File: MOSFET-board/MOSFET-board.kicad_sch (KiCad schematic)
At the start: 64 parts

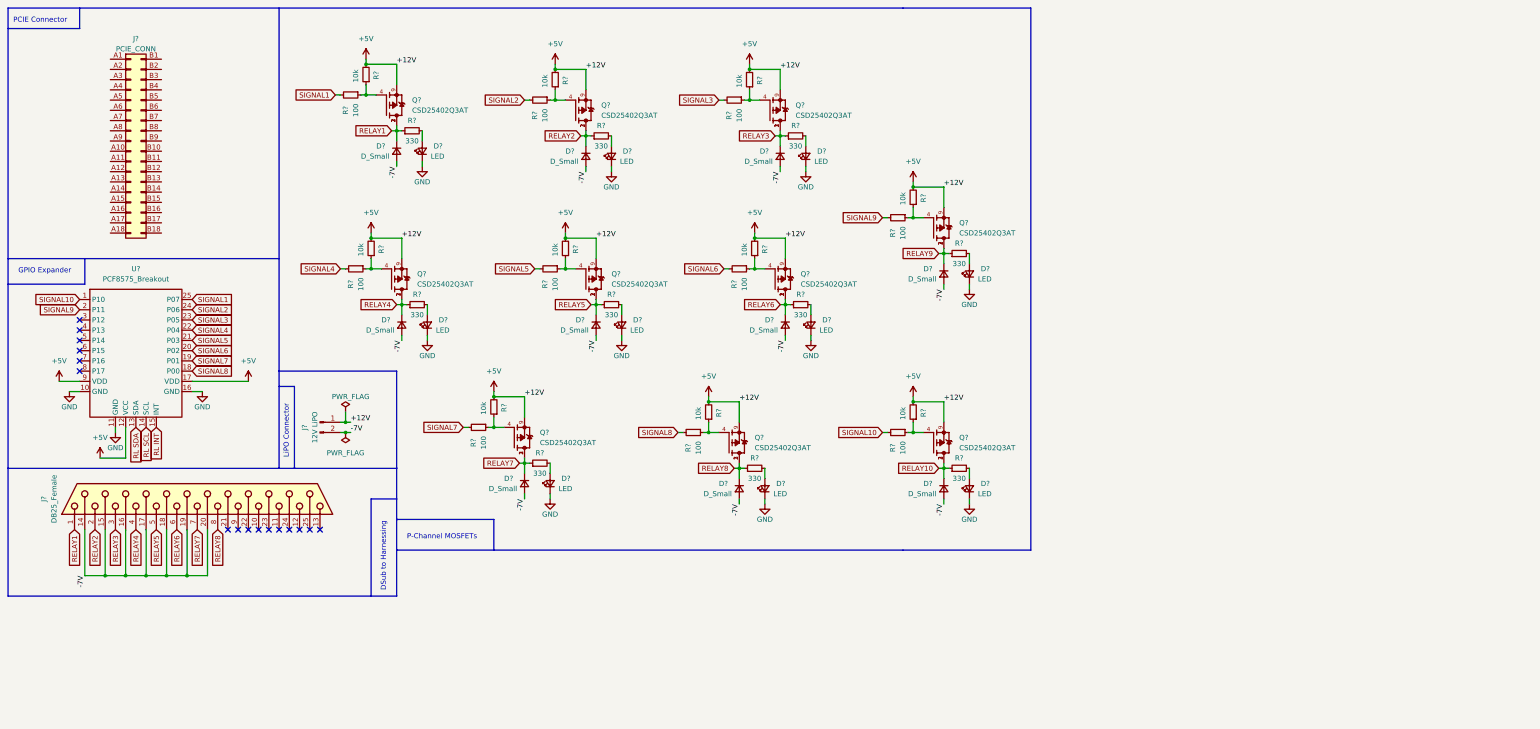
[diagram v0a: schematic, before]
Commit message: Updated mosfet schematics
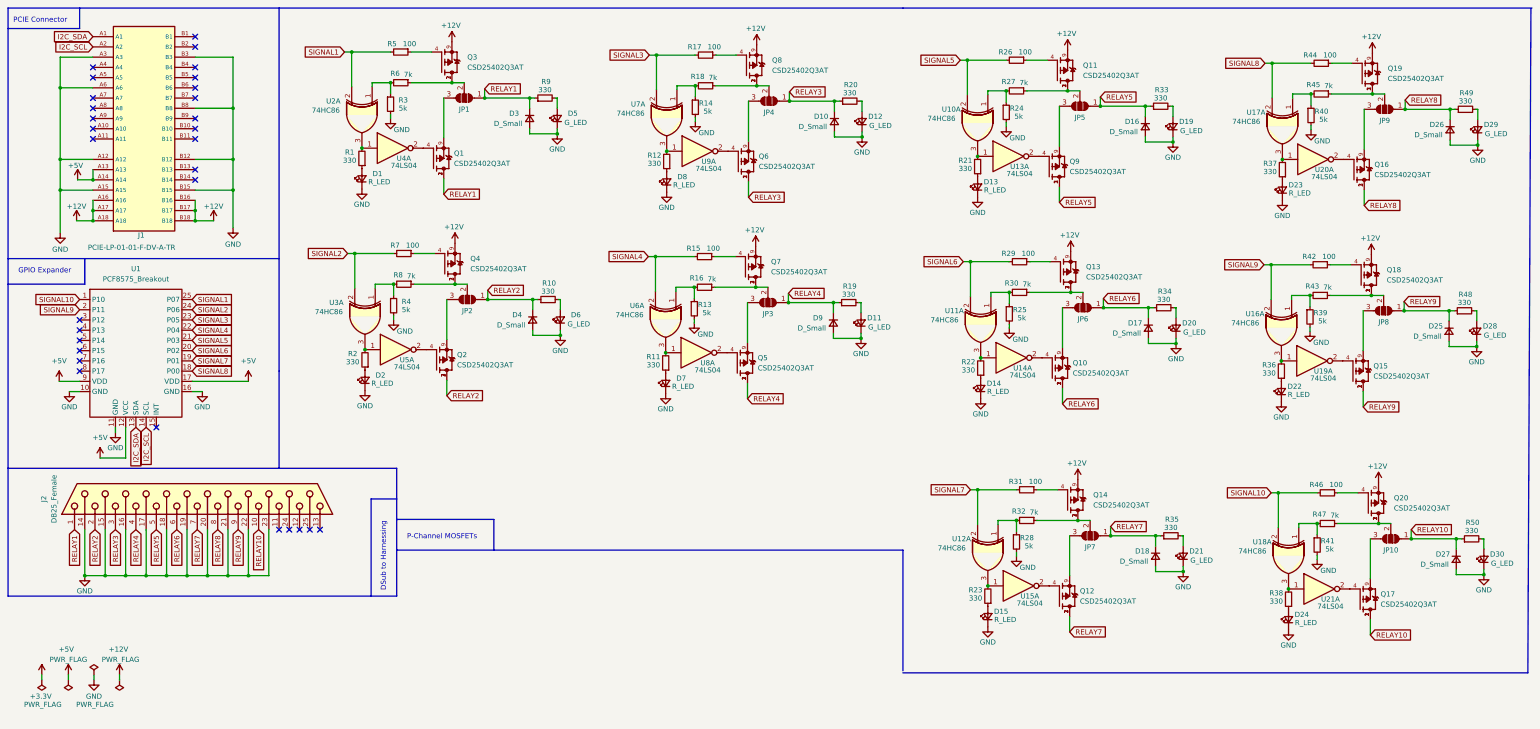
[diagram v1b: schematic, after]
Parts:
- removed D? (x9): LED, LED_THT:LED_D1.8mm_W3.3mm_H2.4mm, symbol Device:LED_Small
- removed D? (x9): D_Small, Diode_THT:D_DO-15_P2.54mm_Vertical_AnodeUp, symbol Device:D_Small
- removed J?: PCIE_CONN, Connector_PCBEdge:BUS_PCIexpress_x1, symbol Connector_Generic:Conn_02x18_Row_Letter_First
- removed J?: 12V LiPO, Connector_PinHeader_2.54mm:PinHeader_1x02_P2.54mm_Vertical, symbol Connector:Conn_01x02_Male
- removed Q? (x9): CSD25402Q3AT, MOSFET:TRANS_CSD25402Q3AT, symbol CSD25402Q3AT:CSD25402Q3AT
- removed R? (x9): 10k, Resistor_SMD:R_0805_2012Metric, symbol Device:R_Small
- removed R? (x9): 330, Resistor_SMD:R_0805_2012Metric, symbol Device:R_Small
- removed R? (x10): 100, Resistor_SMD:R_0805_2012Metric, symbol Device:R_Small
- added D1, D13, D14, D15, D2, D22, D23, D24, D7, D8: R_LED, LED_THT:LED_D1.8mm_W3.3mm_H2.4mm, symbol Device:LED_Small
- added D10, D16, D17, D18, D25, D26, D27, D4, D9: D_Small, Diode_THT:D_DO-15_P2.54mm_Vertical_AnodeUp, symbol Device:D_Small
- added D11, D12, D19, D20, D21, D28, D29, D30, D6: G_LED, LED_THT:LED_D1.8mm_W3.3mm_H2.4mm, symbol Device:LED_Small
- added J1: PCIE-LP-01-01-F-DV-A-TR, PCIe_x1_card_edge:PCIe_x1_card_edge, symbol PCIE_Card_Edge:PCIE-LP-01-01-F-DV-A-TR_(card_edge)
- added JP1, JP10, JP2, JP3, JP4, JP5, JP6, JP7, JP8, JP9: SolderJumper_3_Open, Jumper:SolderJumper-3_P2.0mm_Open_TrianglePad1.0x1.5mm, symbol Jumper:SolderJumper_3_Open
- added Q10, Q11, Q12, Q13, Q14, Q15, Q16, Q17, Q18, Q19, Q2, Q20, Q3, Q4, Q5, Q6, Q7, Q8, Q9: CSD25402Q3AT, MOSFET:TRANS_CSD25402Q3AT, symbol CSD25402Q3AT:CSD25402Q3AT
- added R1, R10, R11, R12, R19, R2, R20, R21, R22, R23, R33, R34, R35, R36, R37, R38, R48, R49, R50: 330, Resistor_SMD:R_0805_2012Metric, symbol Device:R_Small
- added R13, R14, R24, R25, R28, R3, R39, R4, R40, R41: 5k, Resistor_SMD:R_0805_2012Metric, symbol Device:R_Small
- added R15, R17, R26, R29, R31, R42, R44, R46, R7: 100, Resistor_SMD:R_0805_2012Metric, symbol Device:R_Small
- added R16, R18, R27, R30, R32, R43, R45, R47, R6, R8: 7k, Resistor_SMD:R_0805_2012Metric, symbol Device:R_Small
- added U10, U11, U12, U16, U17, U18, U2, U3, U6, U7: 74HC86, symbol 74xx:74HC86
- added U13, U14, U15, U19, U20, U21, U4, U5, U8, U9: 74LS04, symbol 74xx:74LS04
- D5: renamed from D?; value LED -> G_LED
- R5: renamed from R?; value 10k -> 100
- gave numbers to parts that had none: 5
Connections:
- net -7V is gone; now on net GND: D3.2 (A), J2.14 (P14), J2.15 (P15), J2.16 (P16), J2.17 (P17), J2.18 (P18), J2.19 (P19), J2.20 (P20)
- net +5V: now also J1.A13, J1.A14; no longer Q1.9, R5.2
- net GND: now also J2.21 (P21), J2.22 (P22), J2.23 (P23), D1.1 (K), D10.2 (A), D11.1 (K), D12.1 (K), D13.1 (K), D14.1 (K), D15.1 (K), D16.2 (A), D17.2 (A), D18.2 (A), D19.1 (K), D2.1 (K), D20.1 (K), D21.1 (K), D22.1 (K), D23.1 (K), D24.1 (K), D25.2 (A), D26.2 (A), D27.2 (A), D28.1 (K), D29.1 (K), D30.1 (K), D4.2 (A), D6.1 (K), D7.1 (K), D8.1 (K), D9.2 (A), J1.A12, J1.A15, J1.A3, J1.A6, J1.B12, J1.B15, J1.B3, J1.B8, R13.2, R14.2, R24.2, R25.2, R28.2, R3.2, R39.2, R4.2, R40.2, R41.2
- net RELAY1: now also JP1.1 (A)
- net RELAY10: now also J2.10, D27.1 (K), JP10.1 (A), Q17.1, Q17.2, Q17.3, R50.1
- net RELAY2: now also D4.1 (K), JP2.1 (A), Q2.1, Q2.2, Q2.3, R10.1
- net RELAY3: now also D10.1 (K), JP4.1 (A), Q6.1, Q6.2, Q6.3, R20.1
- net RELAY4: now also D9.1 (K), JP3.1 (A), Q5.1, Q5.2, Q5.3, R19.1
- net RELAY5: now also D16.1 (K), JP5.1 (A), Q9.1, Q9.2, Q9.3, R33.1
- net RELAY6: now also D17.1 (K), JP6.1 (A), Q10.1, Q10.2, Q10.3, R34.1
- net RELAY7: now also D18.1 (K), JP7.1 (A), Q12.1, Q12.2, Q12.3, R35.1
- net RELAY8: now also D26.1 (K), JP9.1 (A), Q16.1, Q16.2, Q16.3, R49.1
- net RELAY9: now also J2.9, D25.1 (K), JP8.1 (A), Q15.1, Q15.2, Q15.3, R48.1
- net SIGNAL1: now also R5.2, U2.2
- net SIGNAL10: now also R46.2, U18.2
- net SIGNAL2: now also R7.2, U3.2
- net SIGNAL3: now also R17.2, U7.2
- net SIGNAL4: now also R15.2, U6.2
- net SIGNAL5: now also R26.2, U10.2
- net SIGNAL6: now also R29.2, U11.2
- net SIGNAL7: now also R31.2, U12.2
- net SIGNAL8: now also R44.2, U17.2
- net SIGNAL9: now also R42.2, U16.2
- net at Q1.4: now also U4.2; no longer R5.1
- net RL INT: no longer names the net of U1.15 (INT)
- net RL SCL renamed I2C_SCL
- net I2C_SCL: now also J1.A2
- net RL SDA renamed I2C_SDA
- net I2C_SDA: now also J1.A1
- new net: D30.2 (A), R50.2
- new net: D1.2 (A), R1.1
- new net: JP8.2 (C), Q18.1, Q18.2, Q18.3, R43.1
- new net: JP8.3 (B), Q15.9
- new net: R38.2, U18.3, U21.1
- new net: Q17.4, U21.2
- new net: JP9.2 (C), Q19.1, Q19.2, Q19.3, R45.1
- new net: JP9.3 (B), Q16.9
- new net: D29.2 (A), R49.2
- new net: D28.2 (A), R48.2
- new net: R39.1, R43.2, U16.1
- new net: R24.1, R27.2, U10.1
- new net: R21.2, U10.3, U13.1
- new net: Q11.4, R26.1
- new net: JP3.2 (C), Q7.1, Q7.2, Q7.3, R16.1
- new net: Q7.4, R15.1
- new net: D2.2 (A), R2.1
- new net: R2.2, U3.3, U5.1
- new net: JP10.2 (C), Q20.1, Q20.2, Q20.3, R47.1
- new net: Q20.4, R46.1
- new net: D24.2 (A), R38.1
- new net: Q8.4, R17.1
- new net: JP7.2 (C), Q14.1, Q14.2, Q14.3, R32.1
- new net: Q14.4, R31.1
- new net: R28.1, R32.2, U12.1
- new net: D23.2 (A), R37.1
- new net: R37.2, U17.3, U20.1
- new net: D22.2 (A), R36.1
- new net: R36.2, U16.3, U19.1
- new net: Q15.4, U19.2
- new net: R12.2, U7.3, U9.1
- new net: Q6.4, U9.2
- new net: Q9.4, U13.2
- new net: R25.1, R30.2, U11.1
- new net: JP1.2 (C), Q3.1, Q3.2, Q3.3, R6.1
- new net: JP1.3 (B), Q1.9
- new net: Q19.4, R44.1
- new net: R1.2, U2.3, U4.1
- new net: D8.2 (A), R12.1
- new net: D13.2 (A), R21.1
- new net: D11.2 (A), R19.2
- new net: Q16.4, U20.2
- new net: JP2.2 (C), Q4.1, Q4.2, Q4.3, R8.1
- new net: JP2.3 (B), Q2.9
- new net: R3.1, R6.2, U2.1
- new net: JP6.2 (C), Q13.1, Q13.2, Q13.3, R30.1
- new net: Q13.4, R29.1
- new net: JP5.2 (C), Q11.1, Q11.2, Q11.3, R27.1
- new net: JP5.3 (B), Q9.9
- new net: R13.1, R16.2, U6.1
- new net: R11.2, U6.3, U8.1
- new net: R4.1, R8.2, U3.1
- new net: Q12.4, U15.2
- new net: JP7.3 (B), Q12.9
- new net: R22.2, U11.3, U14.1
- new net: Q10.4, U14.2
- new net: R23.2, U12.3, U15.1
- new net: Q5.4, U8.2
- new net: D19.2 (A), R33.2
- new net: JP4.3 (B), Q6.9
- new net: R40.1, R45.2, U17.1
- new net: D6.2 (A), R10.2
- new net: D7.2 (A), R11.1
- new net: JP6.3 (B), Q10.9
- new net: JP3.3 (B), Q5.9
- new net: Q4.4, R7.1
- new net: D15.2 (A), R23.1
- new net: R41.1, R47.2, U18.1
- new net: Q18.4, R42.1
- new net: D21.2 (A), R35.2
- new net: D12.2 (A), R20.2
- new net: JP10.3 (B), Q17.9
- new net: D14.2 (A), R22.1
- new net: Q3.4, R5.1
- new net: JP4.2 (C), Q8.1, Q8.2, Q8.3, R18.1
- new net: R14.1, R18.2, U7.1
- new net: Q2.4, U5.2
- new net: D20.2 (A), R34.2
- new net +12V: J1.A16, J1.A17, J1.A18, J1.B16, J1.B17, J1.B18, Q11.9, Q13.9, Q14.9, Q18.9, Q19.9, Q20.9, Q3.9, Q4.9, Q7.9, Q8.9
- no-connect marks 16 -> 30
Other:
- note removed: "LiPO Connector"
- moved on the sheet: D3, D5, Q1, R5, R9

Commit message: Replaced mosfet board with Conor's design using BTS3080EJXUMA1. Modified max31855 symbol to have A (separate assembly) reference designator.
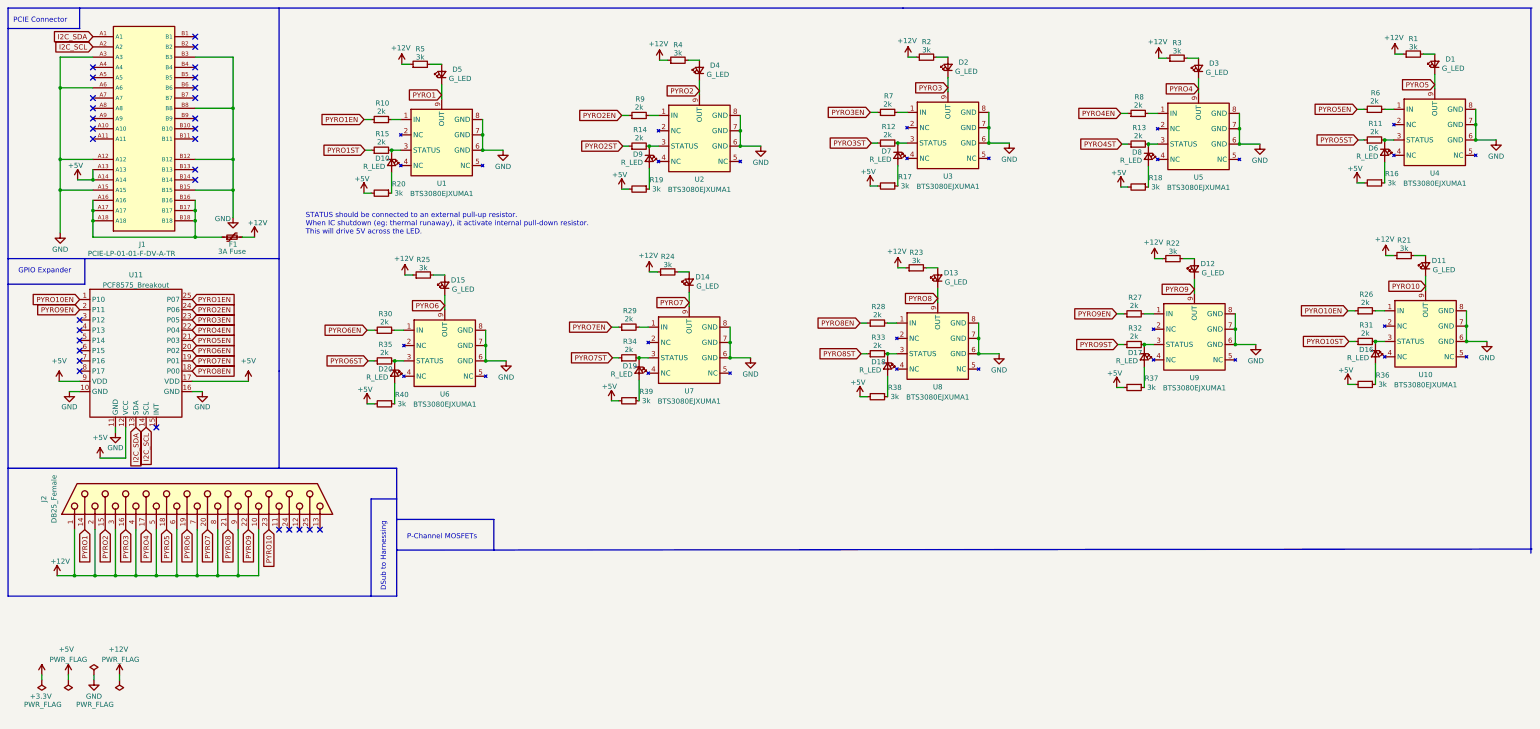
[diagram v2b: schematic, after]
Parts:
- removed D10, D16, D17, D18, D25, D26, D27, D3, D4, D9: D_Small, Diode_THT:D_DO-15_P2.54mm_Vertical_AnodeUp, symbol Device:D_Small
- removed D21, D28, D29, D30: G_LED, LED_THT:LED_D1.8mm_W3.3mm_H2.4mm, symbol Device:LED_Small
- removed D22, D23, D24: R_LED, LED_THT:LED_D1.8mm_W3.3mm_H2.4mm, symbol Device:LED_Small
- removed JP1, JP10, JP2, JP3, JP4, JP5, JP6, JP7, JP8, JP9: SolderJumper_3_Open, Jumper:SolderJumper-3_P2.0mm_Open_TrianglePad1.0x1.5mm, symbol Jumper:SolderJumper_3_Open
- removed Q1, Q10, Q11, Q12, Q13, Q14, Q15, Q16, Q17, Q18, Q19, Q2, Q20, Q3, Q4, Q5, Q6, Q7, Q8, Q9: CSD25402Q3AT, MOSFET:TRANS_CSD25402Q3AT, symbol CSD25402Q3AT:CSD25402Q3AT
- removed R41: 5k, Resistor_SMD:R_0805_2012Metric, symbol Device:R_Small
- removed R42, R44, R46: 100, Resistor_SMD:R_0805_2012Metric, symbol Device:R_Small
- removed R43, R45, R47: 7k, Resistor_SMD:R_0805_2012Metric, symbol Device:R_Small
- removed R48, R49, R50: 330, Resistor_SMD:R_0805_2012Metric, symbol Device:R_Small
- removed U10, U11, U12, U16, U17, U18, U2, U3, U6, U7: 74HC86, symbol 74xx:74HC86
- removed U13, U14, U15, U19, U20, U21, U4, U5, U8, U9: 74LS04, symbol 74xx:74LS04
- added D10, D16, D17, D18, D9: R_LED, LED_THT:LED_D1.8mm_W3.3mm_H2.4mm, symbol Device:LED_Small
- added D3, D4: G_LED, LED_THT:LED_D1.8mm_W3.3mm_H2.4mm, symbol Device:LED_Small
- added F1: 3A Fuse, symbol Device:Polyfuse_Small
- added U1, U10, U2, U3, U4, U5, U6, U7, U8, U9: BTS3080EJXUMA1, BTS3080EJXUMA1:SOIC127P600X115-9N, symbol BTS3080EJXUMA1:BTS3080EJXUMA1
- D1, D13, D14, D15, D2: value R_LED -> G_LED
- D19, D20, D6: value G_LED -> R_LED
- R1, R19, R2, R20, R21, R22, R23, R36, R37, R38: value 330 -> 3k
- R10, R11, R12, R33, R34, R35, R9: value 330 -> 2k
- R13, R14, R28: value 5k -> 2k
- R15, R26, R29, R31, R7: value 100 -> 2k
- R16, R18: value 7k -> 3k
- R17, R5: value 100 -> 3k
- R24, R25, R3, R39, R4, R40: value 5k -> 3k
- R27, R30, R32, R6, R8: value 7k -> 2k
- renumbered U1 to U11
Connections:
- net RELAY10 is gone; now on net +12V: J2.10
- net RELAY8 is gone; now on net +12V: J2.8
- net RELAY9 is gone; now on net +12V: J2.9
- net SIGNAL10 is gone; now on net PYRO10EN: U11.1 (P10)
- net SIGNAL9 is gone; now on net PYRO9EN: U11.2 (P11)
- net +12V: now also J2.1, J2.2, J2.3, J2.4, J2.5, J2.6, J2.7, R1.1, R2.1, R21.1, R22.1, R23.1, R24.1, R25.1, R3.1, R4.1, R5.1, F1.2; no longer J1.A16, J1.A17, J1.A18, J1.B16, J1.B17, J1.B18
- net +5V: now also R16.2, R17.2, R18.2, R19.2, R20.2, R36.2, R37.2, R38.2, R39.2, R40.2
- net GND: now also U1.6 (GND), U1.7 (GND), U1.8 (GND), U10.6 (GND), U10.7 (GND), U10.8 (GND), U2.6 (GND), U2.7 (GND), U2.8 (GND), U3.6 (GND), U3.7 (GND), U3.8 (GND), U4.6 (GND), U4.7 (GND), U4.8 (GND), U5.6 (GND), U5.7 (GND), U5.8 (GND), U6.6 (GND), U6.7 (GND), U6.8 (GND), U7.6 (GND), U7.7 (GND), U7.8 (GND), U8.6 (GND), U8.7 (GND), U8.8 (GND), U9.6 (GND), U9.7 (GND), U9.8 (GND); no longer D1.1 (K), D11.1 (K), D12.1 (K), D13.1 (K), D14.1 (K), D15.1 (K), D19.1 (K), D2.1 (K), D20.1 (K), D5.1 (K), D6.1 (K), D7.1 (K), D8.1 (K), J2.14 (P14), J2.15 (P15), J2.16 (P16), J2.17 (P17), J2.18 (P18), J2.19 (P19), J2.20 (P20), J2.21 (P21), J2.22 (P22), J2.23 (P23), R13.2, R14.2, R24.2, R25.2, R28.2, R3.2, R39.2, R4.2, R40.2
- net at D1.2 (A): now also R1.2; no longer R1.1
- net at R39.1: now also D19.2 (A)
- net at R27.2: now also U9.1 (IN); no longer R24.1
- net at R21.2: now also D11.2 (A)
- net PYRO10EN: now reaches R26.1
- net at R16.1: now also D6.2 (A)
- net PYRO1ST: now reaches R15.1
- net at D2.2 (A): now also R2.2; no longer R2.1
- net at R38.1: now also D18.2 (A)
- net at R17.1: now also D7.2 (A)
- net PYRO9ST: now reaches R32.1
- net PYRO10ST: now reaches R31.1
- net at R32.2: now also D17.1 (K), U9.3 (STATUS); no longer R28.1
- net at R37.1: now also D17.2 (A)
- net at R36.1: now also D16.2 (A)
- net at R12.2: now also D7.1 (K), U3.3 (STATUS)
- net at R30.2: now also U6.1 (IN); no longer R25.1
- net PYRO5EN: now reaches R6.1
- net PYRO5EN: now also U11.21 (P03)
- net at D8.2 (A): now also R18.1; no longer R12.1
- net at D13.2 (A): now also R23.2; no longer R21.1
- net PYRO4EN: now reaches R8.1
- net PYRO4EN: now also U11.22 (P04)
- net at R6.2: now also U4.1 (IN); no longer R3.1
- net PYRO6EN: now reaches R30.1
- net PYRO6EN: now also U11.20 (P02)
- net PYRO7EN: now reaches R29.1
- net PYRO7EN: now also U11.19 (P01)
- net PYRO9EN: now reaches R27.1
- net PYRO4ST: now reaches R13.1
- net PYRO4ST: no longer R16.2
- net at R11.2: now also D6.1 (K), U4.3 (STATUS)
- net at R8.2: now also U5.1 (IN); no longer R4.1
- net at R22.2: now also D12.2 (A)
- net at R33.2: now also D18.1 (K), U8.3 (STATUS); no longer D19.2 (A)
- net at R40.1: now also D20.2 (A)
- net at R10.2: now also U1.1 (IN); no longer D6.2 (A)
- net PYRO5ST: now reaches R11.1
- net PYRO5ST: no longer D7.2 (A)
- net PYRO3EN: now reaches R7.1
- net PYRO3EN: now also U11.23 (P05)
- net at D15.2 (A): now also R25.2; no longer R23.1
- net at R35.2: now also D20.1 (K), U6.3 (STATUS)
- net at R9.2: now also U2.1 (IN); no longer D5.2 (A)
- net at D14.2 (A): now also R24.2; no longer R22.1
- net PYRO2ST: now reaches R14.1
- net PYRO2ST: no longer R18.2
- net at R34.2: now also D19.1 (K), U7.3 (STATUS); no longer D20.2 (A)
- net RELAY1 renamed PYRO2EN
- net PYRO2EN: now also U11.24 (P06); no longer J2.1
- net RELAY2 renamed PYRO1EN
- net PYRO1EN: now also U11.25 (P07); no longer J2.2
- net RELAY3: no longer names the net of R20.1
- net RELAY3: now also D10.2 (A); no longer J2.3
- net RELAY4: no longer names the net of R19.1
- net RELAY4: now also D9.2 (A); no longer J2.4
- net RELAY5 renamed PYRO8ST
- net PYRO8ST: no longer J2.5
- net RELAY6 renamed PYRO7ST
- net PYRO7ST: no longer J2.6
- net RELAY7 renamed PYRO6ST
- net PYRO6ST: no longer J2.7
- net SIGNAL1: no longer names the net of R5.2
- net SIGNAL1: now also D5.2 (A); no longer U11.25 (P07)
- net SIGNAL2: no longer names the net of R7.2
- net SIGNAL2: now also U3.1 (IN); no longer U11.24 (P06)
- removed net SIGNAL3: R17.2, U11.23 (P05)
- net SIGNAL4: no longer names the net of R15.2
- net SIGNAL4: now also D10.1 (K), U1.3 (STATUS); no longer U11.22 (P04)
- net SIGNAL5: no longer names the net of R26.2
- net SIGNAL5: now also U10.1 (IN); no longer U11.21 (P03)
- net SIGNAL6: no longer names the net of R29.2
- net SIGNAL6: now also U7.1 (IN); no longer U11.20 (P02)
- net SIGNAL7: no longer names the net of R31.2
- net SIGNAL7: now also D16.1 (K), U10.3 (STATUS); no longer U11.19 (P01)
- net SIGNAL8 renamed PYRO8EN
- net PYRO8EN: now also R28.1
- new net: D9.1 (K), R14.2, U2.3 (STATUS)
- new net: D4.2 (A), R4.2
- new net: D8.1 (K), R13.2, U5.3 (STATUS)
- new net: F1.1, J1.A16, J1.A17, J1.A18, J1.B16, J1.B17, J1.B18
- new net: D3.2 (A), R3.2
- new net: R28.2, U8.1 (IN)
- new net PYRO1: D5.1 (K), J2.14 (P14), U1.9 (OUT)
- new net PYRO10: D11.1 (K), J2.23 (P23), U10.9 (OUT)
- new net PYRO2: D4.1 (K), J2.15 (P15), U2.9 (OUT)
- new net PYRO3: D2.1 (K), J2.16 (P16), U3.9 (OUT)
- new net PYRO3ST: R12.1
- new net PYRO4: D3.1 (K), J2.17 (P17), U5.9 (OUT)
- new net PYRO5: D1.1 (K), J2.18 (P18), U4.9 (OUT)
- new net PYRO6: D15.1 (K), J2.19 (P19), U6.9 (OUT)
- new net PYRO7: D14.1 (K), J2.20 (P20), U7.9 (OUT)
- new net PYRO8: D13.1 (K), J2.21 (P21), U8.9 (OUT)
- new net PYRO9: D12.1 (K), J2.22 (P22), U9.9 (OUT)
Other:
- note added: "STATUS should be connected to an external pull-up resistor. When IC shutdown (eg: thermal runaway), it activate internal pull-down resistor. This will drive 5V across the LED."
